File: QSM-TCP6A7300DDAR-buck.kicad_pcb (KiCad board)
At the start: 2 copper layers, 45 x 30 mm, 0 parts

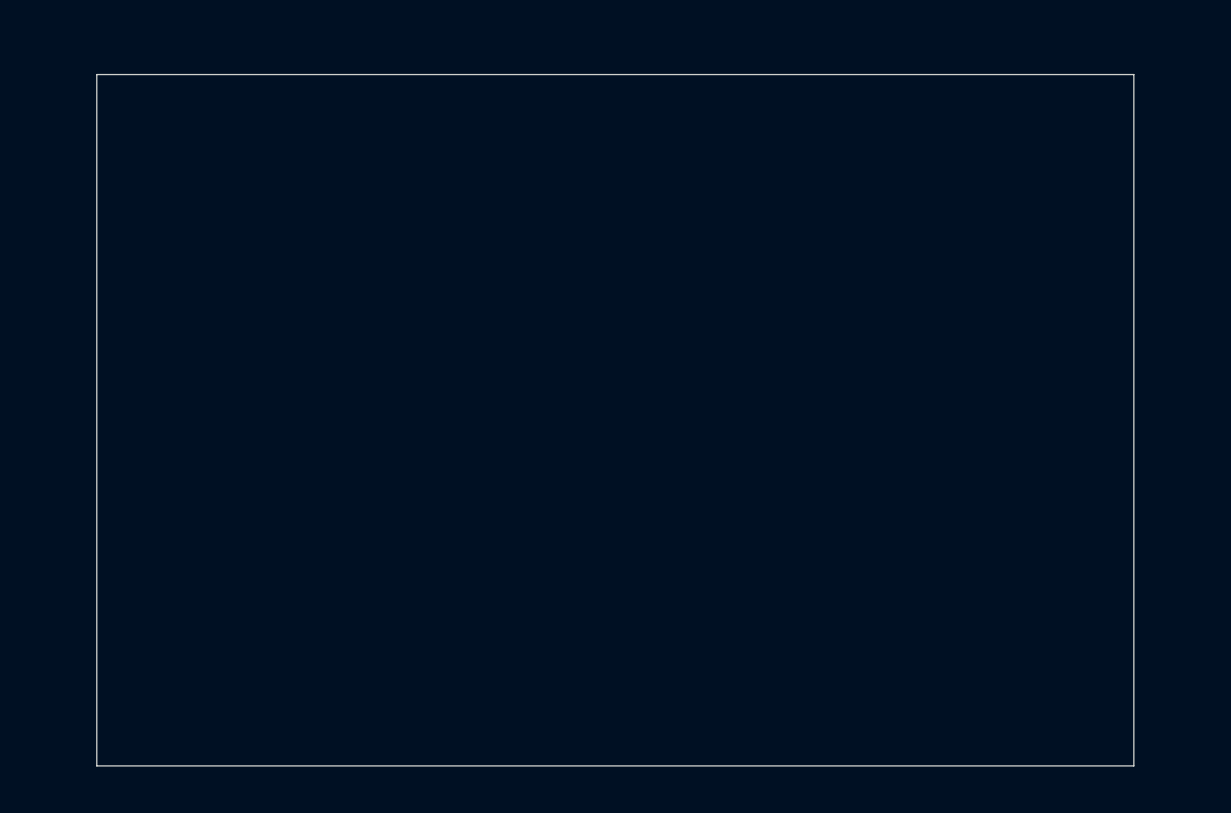
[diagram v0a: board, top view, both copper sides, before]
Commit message: feat(layout): [WIP] ruteo inicial de polígonos de potencia en 4 capas
Se definió el stackup simétrico de 4 capas (SIG-GND-GND-SIG) y se realizó el floorplanning. Se trazaron los polígonos preliminares de alta corriente (VIN, SW, VOUT) en la capa Top. El ruteo de la señal de Feedback y los planos de tierra internos siguen en progreso.
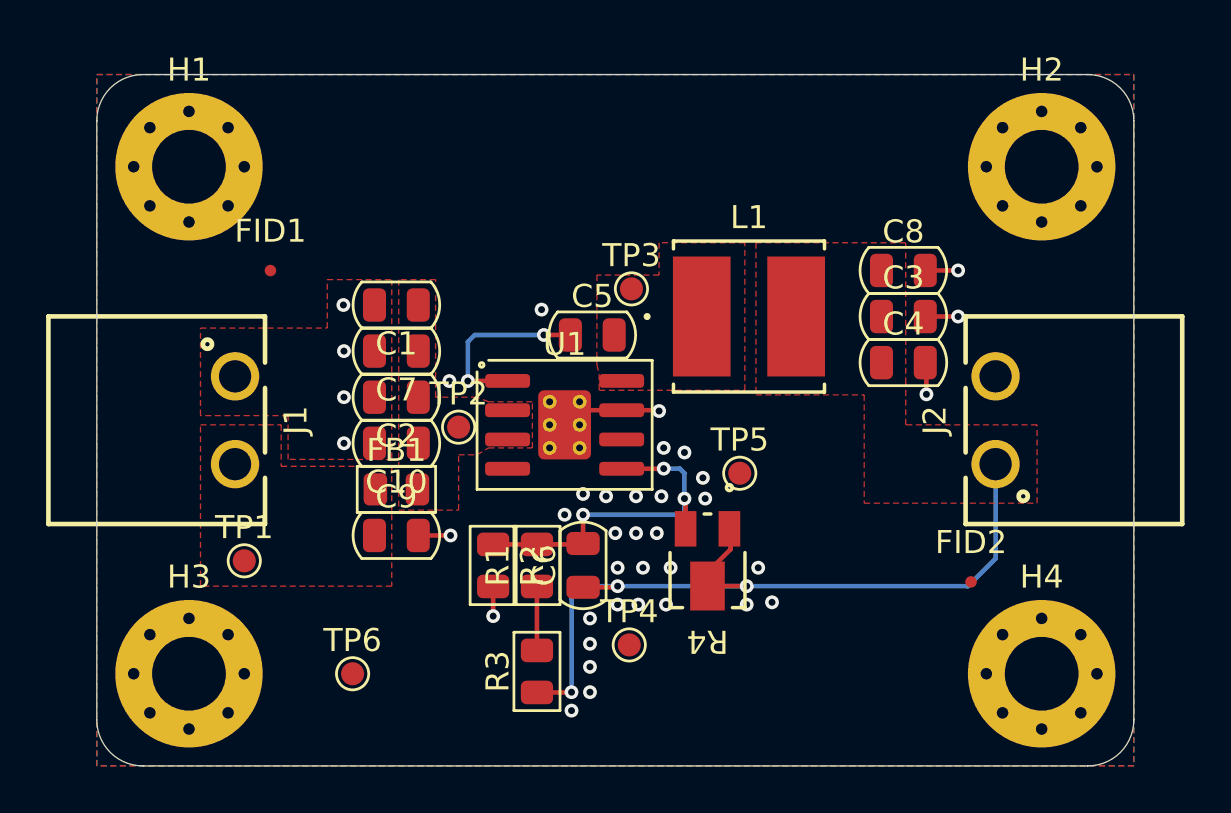
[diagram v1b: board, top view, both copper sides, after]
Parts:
- added C1: 0.1uF, Capacitor_SMD_ARR:C_0805_2012Metric, F.Cu at (113.0, 80.0)
- added C10: 0.1uF, Capacitor_SMD_ARR:C_0805_2012Metric, F.Cu at (113.0, 86.0)
- added C2: 2.2uF, Capacitor_SMD_ARR:C_0805_2012Metric, F.Cu at (113.0, 84.0)
- added C3: 10uF, Capacitor_SMD_ARR:C_0805_2012Metric, F.Cu at (135.0, 80.5)
- added C4: 0.1uF, Capacitor_SMD_ARR:C_0805_2012Metric, F.Cu at (135.0, 82.5)
- added C5: 0.1uF, Capacitor_SMD_ARR:C_0805_2012Metric, F.Cu at (121.5, 81.3)
- added C6: 100pF, Capacitor_SMD_ARR:C_0805_2012Metric, F.Cu at (121.1, 91.3)
- added C7: 1uF, Capacitor_SMD_ARR:C_0805_2012Metric, F.Cu at (113.0, 82.0)
- added C8: 1uF, Capacitor_SMD_ARR:C_0805_2012Metric, F.Cu at (135.0, 78.5)
- added C9: 0.1uF, Capacitor_SMD_ARR:C_0805_2012Metric, F.Cu at (113.0, 90.0)
- added FB1: ~, Resistor_SMD_ARR:R_0805_2012Metric, F.Cu at (113.0, 88.0)
- added FID1: Fiducial, Fiducial_ARR:Fiducial_0.5mm_Mask1.5mm, F.Cu at (107.5, 78.5)
- added FID2: Fiducial, Fiducial_ARR:Fiducial_0.5mm_Mask1.5mm, F.Cu at (137.9, 92.0)
- added H1: MountingHole, Mounting_Hole_ARR:MountingHole_3.2mm_M3_Pad_Via, F.Cu at (104.0, 74.0)
- added H2: MountingHole, Mounting_Hole_ARR:MountingHole_3.2mm_M3_Pad_Via, F.Cu at (141.0, 74.0)
- added H3: MountingHole, Mounting_Hole_ARR:MountingHole_3.2mm_M3_Pad_Via, F.Cu at (104.0, 96.0)
- added H4: MountingHole, Mounting_Hole_ARR:MountingHole_3.2mm_M3_Pad_Via, F.Cu at (141.0, 96.0)
- added J1: 691322310002, Connector_THT_ARR:691322310002, F.Cu at (106.0, 85.0)
- added J2: 691322310002, Connector_THT_ARR:691322310002, F.Cu at (139.0, 85.0)
- added L1: 10uH, IND_SMD_ARR:IND_SWPA6020S_SNL, F.Cu at (128.3, 80.5)
- added R1: 56K, Resistor_SMD_ARR:R_0805_2012Metric, F.Cu at (119.1, 91.3)
- added R2: 10K, Resistor_SMD_ARR:R_0805_2012Metric, F.Cu at (117.2, 91.3)
- added R3: 0R, Resistor_SMD_ARR:R_0805_2012Metric, F.Cu at (119.1, 95.9)
- added R4: 100K, Resistor_THT_ARR:POT_TC33_3X3P8_BRN, F.Cu at (126.5, 91.1)
- added TP1: TestPoint, Test_Point_ARR:TestPoint_Pad_D1.0mm, F.Cu at (106.4, 91.1)
- added TP2: TestPoint, Test_Point_ARR:TestPoint_Pad_D1.0mm, F.Cu at (115.7, 85.3)
- added TP3: TestPoint, Test_Point_ARR:TestPoint_Pad_D1.0mm, F.Cu at (123.2, 79.3)
- added TP4: TestPoint, Test_Point_ARR:TestPoint_Pad_D1.0mm, F.Cu at (123.1, 94.8)
- added TP5: TestPoint, Test_Point_ARR:TestPoint_Pad_D1.0mm, F.Cu at (127.9, 87.3)
- added TP6: TestPoint, Test_Point_ARR:TestPoint_Pad_D1.0mm, F.Cu at (111.1, 96.0)
- added U1: TCP6A7300DDAR, Package_SO_ARR:SOIC-8-1EP_3.9x4.9mm_P1.27mm_EP2.29x3mm_ThermalVias, F.Cu at (120.3, 85.2)
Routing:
- net Net-(C3-Pad1): track 0.00 -> 34.9 mm, vias 0 -> 3
- net Net-(U1-FB): track 0.00 -> 15.5 mm, vias 0 -> 3
- net GND: track 0.00 -> 10.3 mm, vias 0 -> 38
- net Net-(U1-BOOT): track 0.00 -> 8.00 mm, vias 0 -> 2
- net Net-(R1-Pad1): track 0.00 -> 2.77 mm
- added copper zone on B.Cu, net GND
- added copper zone on F.Cu, net GND
- added copper zone on In1.Cu, net GND
- added copper zone on In2.Cu, net GND
- added copper zone on F.Cu, net Net-(C3-Pad1)
- added copper zone on F.Cu, net Net-(C9-Pad1)
- added copper zone on F.Cu, net Net-(U1-EN)
- added copper zone on F.Cu, net Net-(U1-SW)
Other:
- outline, holes or cut-outs redrawn
- copper layers 2 -> 4

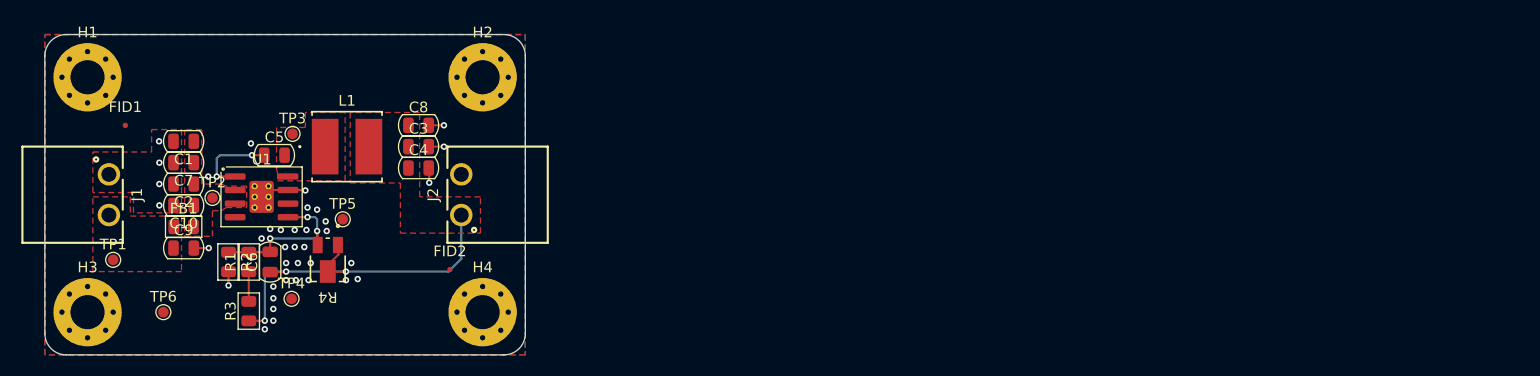
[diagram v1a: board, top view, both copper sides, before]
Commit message: feat(hardware): optimización de hot-loops, conector de inyección de señal y actualización de docs
Esquemático y PCB:
- Reubicación jerárquica de capacitores de entrada y salida para minimizar el área del Hot Loop y reducir el ESL, alineado a notas de aplicación de PI.
- Adición de conector SMD JST SH (BM02B-SRSS-TB) en paralelo a la resistencia de inyección para facilitar la medición del lazo de control (Bode Plot).

Documentación (README):
- Integración de 'badges' de estado y especificaciones técnicas.
- Redacción de la justificación técnica del layout (Control EMI y Hot Loops) referenciando bibliografía de TI.
- Adición de render 3D de la placa y diagrama esquemático de la aplicación típica.
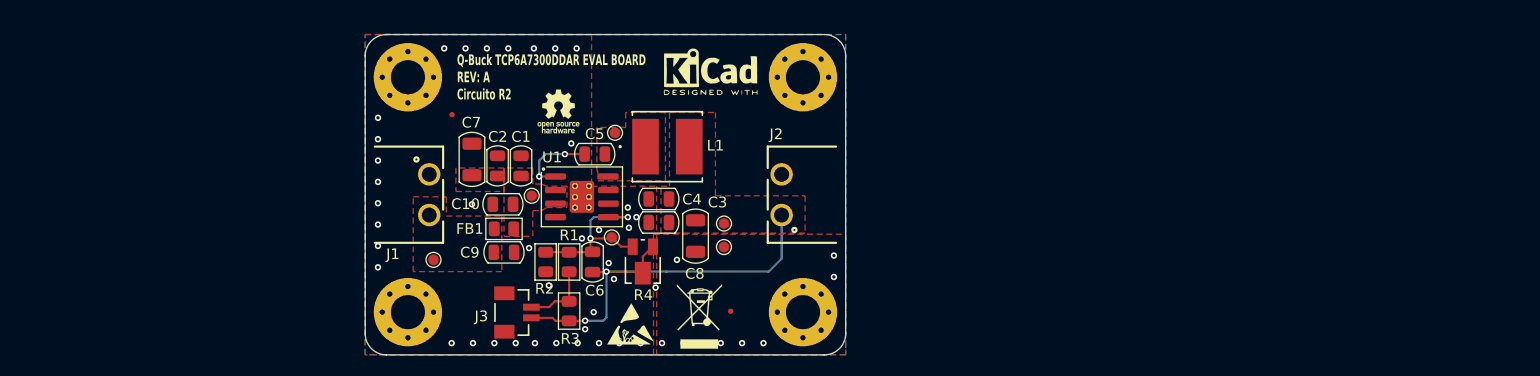
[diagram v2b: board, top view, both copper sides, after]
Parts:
- added G***: LOGO, LOGO, F.Cu at (155.0, 97.2)
- added G***: LOGO, LOGO, F.Cu at (162.3, 73.5)
- added J3: BM02B-SRSS-TB LFSN, Connector_SMD_ARR:BM02B-SRSS-TB_JST, F.Cu at (143.7, 96.0)
- added REF**: OSHW-Logo_5.7x6mm_SilkScreen, Symbol_ARR:OSHW-Logo_5.7x6mm_SilkScreen, F.Cu at (148.1, 77.2)
- added REF**: WEEE-Logo_4.2x6mm_SilkScreen, Symbol_ARR:WEEE-Logo_4.2x6mm_SilkScreen, F.Cu at (161.3, 96.4)
- C7, C8: value 1uF -> 10uF; footprint Capacitor_SMD_ARR:C_0805_2012Metric -> Capacitor_SMD_ARR:C_1206_3216Metric
- moved TP6 52.9 mm to (163.6, 89.9)
- moved TP4 41.1 mm to (163.6, 87.7)
- moved C1 31.7 mm to (144.6, 82.3), turned to 90 degrees
- moved FID1 30.6 mm to (138.1, 77.5)
- moved TP3 30.2 mm to (153.4, 79.2)
- moved C6 30.2 mm to (151.3, 91.3)
- moved C9 30.0 mm to (143.0, 90.4)
- moved FB1 30.0 mm to (143.0, 88.2)
- moved C5 30.0 mm to (151.5, 81.2)
- moved U1 30.0 mm to (150.3, 85.2)
- moved H1 30.0 mm to (134.0, 74.0)
- moved H2 30.0 mm to (171.0, 74.0)
- moved H3 30.0 mm to (134.0, 96.0)
- moved H4 30.0 mm to (171.0, 96.0)
- moved J1 30.0 mm to (136.0, 85.0)
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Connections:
- H1 pad 1: unconnected-(H1-Pad1)_7 -> GND
- H2 pad 1: unconnected-(H2-Pad1)_4 -> GND
- H3 pad 1: unconnected-(H3-Pad1)_3 -> GND
- H4 pad 1: unconnected-(H4-Pad1) -> GND
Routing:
- net GND: track 10.3 -> 0.00 mm, vias 38 -> 48
- net Net-(C3-Pad1): track 34.9 -> 40.4 mm, vias 3 -> 2
- net Net-(J3-Pad1): track 2.77 -> 6.54 mm
- net Net-(U1-FB): track 15.5 -> 16.5 mm, vias 3 -> 2
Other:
- board text added: "${TITLE} REV: ${REVISION} ${COMPANY}"

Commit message: chore(project): preparación para manufactura (BOM, stackup PCB y docs)
Documentación (README):
- Refactorización de la narrativa del proyecto enfocándose en la validación empírica y el desarrollo de la industria nacional.
- Integración de la sección 'Design for Testability' (DFT) y justificación técnica del stackup de 4 capas.

Layout (PCB):
- Adición de las tablas de características de la placa y detalles del stackup (capas, grosores de FR4/Prepreg y cobre) en la capa de dibujo para referencia del fabricante.

Proyecto y Esquemático:
- Ajuste y actualización de los metadatos de los componentes para habilitar una generación de BOM limpia y automatizada.
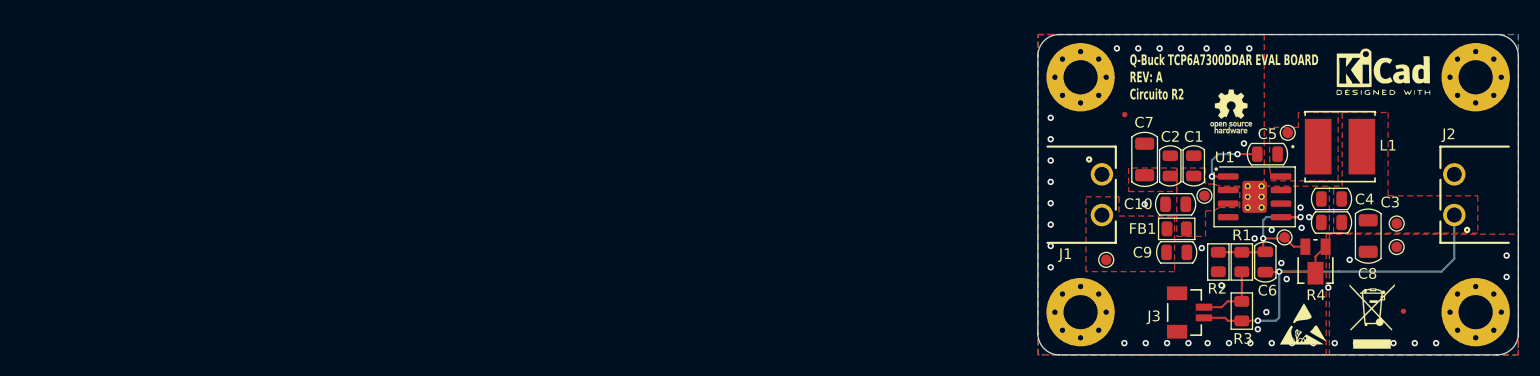
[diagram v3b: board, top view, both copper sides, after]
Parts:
- moved C1 63.0 mm to (207.6, 82.3)
- moved C10 63.0 mm to (205.9, 85.9)
- moved C2 63.0 mm to (205.4, 82.3)
- moved C3 63.0 mm to (220.5, 87.6)
- moved C4 63.0 mm to (220.5, 85.4)
- moved C5 63.0 mm to (214.5, 81.2)
- moved C6 63.0 mm to (214.3, 91.3)
- moved C7 63.0 mm to (203.0, 81.7)
- moved C8 63.0 mm to (223.9, 88.9)
- moved C9 63.0 mm to (206.0, 90.4)
- moved FB1 63.0 mm to (206.0, 88.2)
- moved FID1 63.0 mm to (201.1, 77.5)
- moved FID2 63.0 mm to (227.2, 95.9)
- moved G*** 63.0 mm to (218.0, 97.2)
- moved G*** 63.0 mm to (225.3, 73.5)
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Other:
- board text added: "A MENOS QUE SE ESPECIFIQUE LO CONTRARIO, ESTA PLACA IMPRESA DEBERÁ FABRICARSE DE ACUERDO CON LOS SIGUIENTES ESTÁNDARES IPC: - IPC-A-600 CLASE 2 (CRITERIOS DE ACEPTABILIDAD). - IPC-6012 CLASE 2 (CALIFICACIÓN Y RENDIMIENTO PARA PLACAS IMPRESAS RÍGIDAS). - LOS MATERIALES DEBEN CUMPLIR CON IPC-4101."
